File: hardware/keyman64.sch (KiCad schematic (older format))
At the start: 28 parts, among them IC1 ATMEGA1284P-P, P1 SERIAL, P2 CIA1, P3 KEYBOARD, P4 USER, P6 USB, SW1 RESET, SW2 BOOTLOADER, SW3 POWER, U1 7400, U2 ICL7660, U3 4520, U4 4051, U5 4051, U6 CD74HC22106, X1 16Mhz

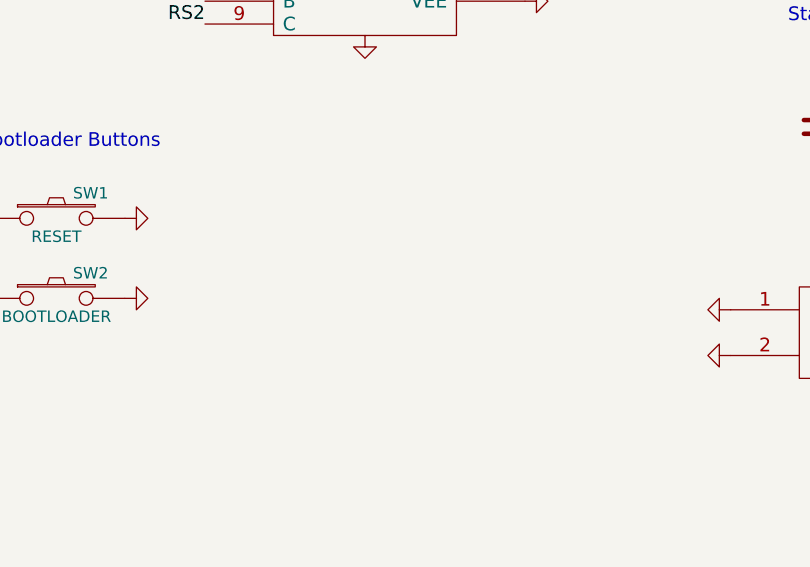
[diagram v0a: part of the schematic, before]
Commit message: Hardware: Increased board height to 6,4cm to make room for mounting holes
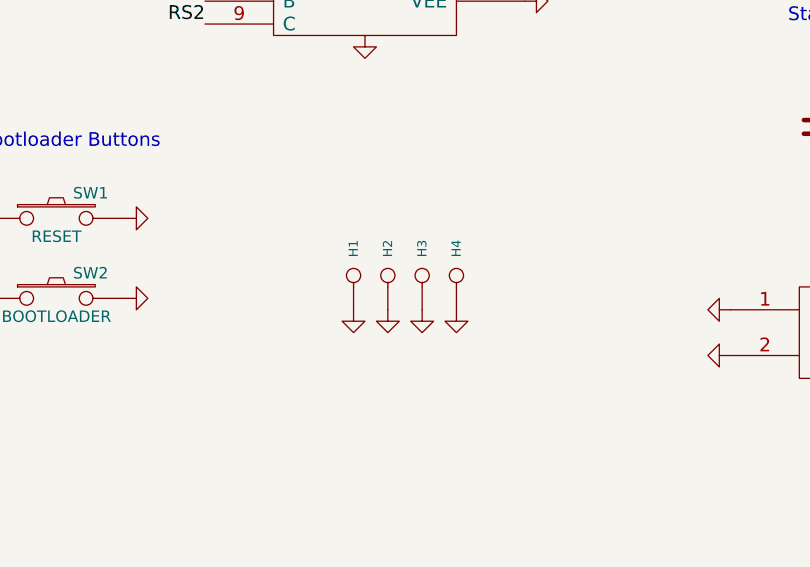
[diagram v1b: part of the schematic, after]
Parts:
- added H1, H2, H3, H4: CONN_1, symbol CONN_1
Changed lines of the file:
@@
 Sheet 1 1
 Title "Programmable C64 Keyboard Interceptor and Hardware Controller"
-Date "23 oct 2015"
+Date "24 oct 2015"
 Rev "2"
 Comp "Henning Bekel"
@@
 Text Label 900  2950 2    60   ~ 0
 KVCC
+$Comp
+L CONN_1 H1
+U 1 1 562B9608
+P 8150 6500
+F 0 "H1" H 8230 6500 40  0000 L CNN
+F 1 "CONN_1" H 8150 6555 30  0001 C CNN
+F 2 "" H 8150 6500 60  0000 C CNN
+F 3 "" H 8150 6500 60  0000 C CNN
+	1    8150 6500
+	0    -1   -1   0
+$EndComp
+$Comp
+L GND #PWR046
+U 1 1 562B9617
+P 8150 6650
+F 0 "#PWR046" H 8150 6650 30  0001 C CNN
+F 1 "GND" H 8150 6580 30  0001 C CNN
+F 2 "" H 8150 6650 60  0000 C CNN
+F 3 "" H 8150 6650 60  0000 C CNN
+	1    8150 6650
+	1    0    0    -1
+$EndComp
+$Comp
+L CONN_1 H2
+U 1 1 562B962E
+P 8300 6500
+F 0 "H2" H 8380 6500 40  0000 L CNN
+F 1 "CONN_1" H 8300 6555 30  0001 C CNN
+F 2 "" H 8300 6500 60  0000 C CNN
+F 3 "" H 8300 6500 60  0000 C CNN
+	1    8300 6500
+	0    -1   -1   0
+$EndComp
+$Comp
+L GND #PWR047
+U 1 1 562B9634
+P 8300 6650
+F 0 "#PWR047" H 8300 6650 30  0001 C CNN
+F 1 "GND" H 8300 6580 30  0001 C CNN
+F 2 "" H 8300 6650 60  0000 C CNN
+F 3 "" H 8300 6650 60  0000 C CNN
+	1    8300 6650
+	1    0    0    -1
+$EndComp
+$Comp
+L CONN_1 H3
+U 1 1 562B963A
+P 8450 6500
+F 0 "H3" H 8530 6500 40  0000 L CNN
+F 1 "CONN_1" H 8450 6555 30  0001 C CNN
+F 2 "" H 8450 6500 60  0000 C CNN
+F 3 "" H 8450 6500 60  0000 C CNN
+	1    8450 6500
+	0    -1   -1   0
+$EndComp
+$Comp
+L GND #PWR048
+U 1 1 562B9640
+P 8450 6650
+F 0 "#PWR048" H 8450 6650 30  0001 C CNN
+F 1 "GND" H 8450 6580 30  0001 C CNN
+F 2 "" H 8450 6650 60  0000 C CNN
+F 3 "" H 8450 6650 60  0000 C CNN
+	1    8450 6650
+	1    0    0    -1
+$EndComp
+$Comp
+L CONN_1 H4
+U 1 1 562B9646
+P 8600 6500
+F 0 "H4" H 8680 6500 40  0000 L CNN
+F 1 "CONN_1" H 8600 6555 30  0001 C CNN
+F 2 "" H 8600 6500 60  0000 C CNN
+F 3 "" H 8600 6500 60  0000 C CNN
+	1    8600 6500
+	0    -1   -1   0
+$EndComp
+$Comp
+L GND #PWR049
+U 1 1 562B964C
+P 8600 6650
+F 0 "#PWR049" H 8600 6650 30  0001 C CNN
+F 1 "GND" H 8600 6580 30  0001 C CNN
+F 2 "" H 8600 6650 60  0000 C CNN
+F 3 "" H 8600 6650 60  0000 C CNN
+	1    8600 6650
+	1    0    0    -1
+$EndComp
 $EndSCHEMATC

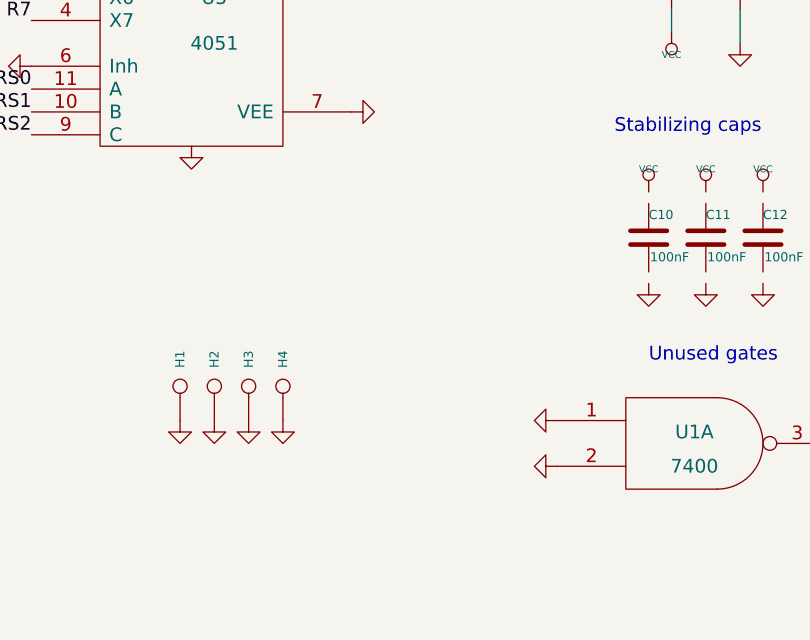
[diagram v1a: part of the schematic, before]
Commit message: Hardware: Rearranged parts, more caps, rerouted (first rough draft)
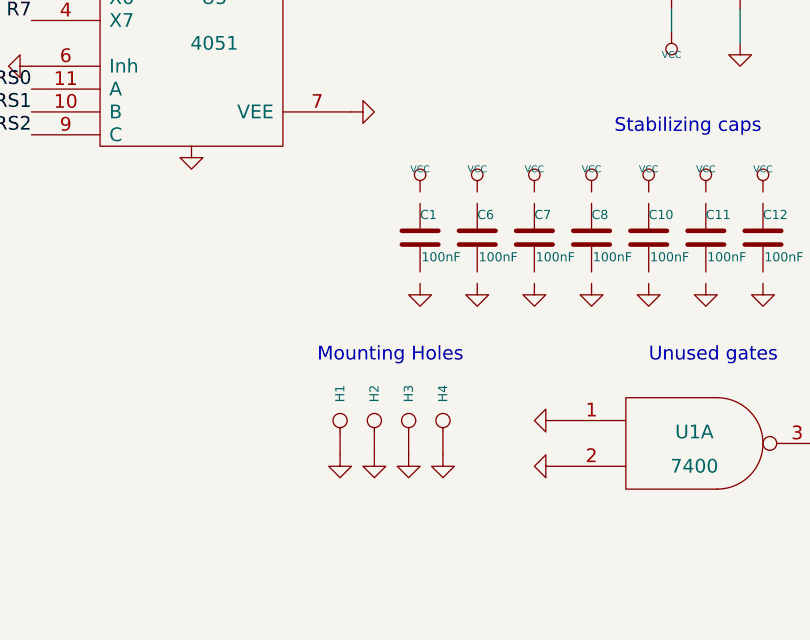
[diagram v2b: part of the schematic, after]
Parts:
- added C1, C6, C7, C8: 100nF, ~, symbol C
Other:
- note added: "Mounting Holes"
- moved on the sheet: H1, H2, H3, H4
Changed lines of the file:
@@
 Sheet 1 1
 Title "Programmable C64 Keyboard Interceptor and Hardware Controller"
-Date "24 oct 2015"
+Date "27 oct 2015"
 Rev "2"
 Comp "Henning Bekel"
@@
 	1    0    0    -1
 $EndComp
-NoConn ~ 900  2200
 Text Label 900  2000 2    60   ~ 0
 D-
@@
 L CONN_1 H1
 U 1 1 562B9608
-P 8150 6500
-F 0 "H1" H 8230 6500 40  0000 L CNN
-F 1 "CONN_1" H 8150 6555 30  0001 C CNN
-F 2 "" H 8150 6500 60  0000 C CNN
-F 3 "" H 8150 6500 60  0000 C CNN
-	1    8150 6500
+P 8850 6650
+F 0 "H1" H 8930 6650 40  0000 L CNN
+F 1 "CONN_1" H 8850 6705 30  0001 C CNN
+F 2 "" H 8850 6650 60  0000 C CNN
+F 3 "" H 8850 6650 60  0000 C CNN
+	1    8850 6650
 	0    -1   -1   0
 $EndComp
@@
 L GND #PWR046
 U 1 1 562B9617
-P 8150 6650
-F 0 "#PWR046" H 8150 6650 30  0001 C CNN
-F 1 "GND" H 8150 6580 30  0001 C CNN
-F 2 "" H 8150 6650 60  0000 C CNN
-F 3 "" H 8150 6650 60  0000 C CNN
-	1    8150 6650
+P 8850 6800
+F 0 "#PWR046" H 8850 6800 30  0001 C CNN
+F 1 "GND" H 8850 6730 30  0001 C CNN
+F 2 "" H 8850 6800 60  0000 C CNN
+F 3 "" H 8850 6800 60  0000 C CNN
+	1    8850 6800
 	1    0    0    -1
 $EndComp
@@
 L CONN_1 H2
 U 1 1 562B962E
-P 8300 6500
-F 0 "H2" H 8380 6500 40  0000 L CNN
-F 1 "CONN_1" H 8300 6555 30  0001 C CNN
-F 2 "" H 8300 6500 60  0000 C CNN
-F 3 "" H 8300 6500 60  0000 C CNN
-	1    8300 6500
+P 9000 6650
+F 0 "H2" H 9080 6650 40  0000 L CNN
+F 1 "CONN_1" H 9000 6705 30  0001 C CNN
+F 2 "" H 9000 6650 60  0000 C CNN
+F 3 "" H 9000 6650 60  0000 C CNN
+	1    9000 6650
 	0    -1   -1   0
 $EndComp
@@
 L GND #PWR047
 U 1 1 562B9634
-P 8300 6650
-F 0 "#PWR047" H 8300 6650 30  0001 C CNN
-F 1 "GND" H 8300 6580 30  0001 C CNN
-F 2 "" H 8300 6650 60  0000 C CNN
-F 3 "" H 8300 6650 60  0000 C CNN
-	1    8300 6650
+P 9000 6800
+F 0 "#PWR047" H 9000 6800 30  0001 C CNN
+F 1 "GND" H 9000 6730 30  0001 C CNN
+F 2 "" H 9000 6800 60  0000 C CNN
+F 3 "" H 9000 6800 60  0000 C CNN
+	1    9000 6800
 	1    0    0    -1
 $EndComp
@@
 L CONN_1 H3
 U 1 1 562B963A
-P 8450 6500
-F 0 "H3" H 8530 6500 40  0000 L CNN
-F 1 "CONN_1" H 8450 6555 30  0001 C CNN
-F 2 "" H 8450 6500 60  0000 C CNN
-F 3 "" H 8450 6500 60  0000 C CNN
-	1    8450 6500
+P 9150 6650
+F 0 "H3" H 9230 6650 40  0000 L CNN
+F 1 "CONN_1" H 9150 6705 30  0001 C CNN
+F 2 "" H 9150 6650 60  0000 C CNN
+F 3 "" H 9150 6650 60  0000 C CNN
+	1    9150 6650
 	0    -1   -1   0
 $EndComp
@@
 L GND #PWR048
 U 1 1 562B9640
-P 8450 6650
-F 0 "#PWR048" H 8450 6650 30  0001 C CNN
-F 1 "GND" H 8450 6580 30  0001 C CNN
-F 2 "" H 8450 6650 60  0000 C CNN
-F 3 "" H 8450 6650 60  0000 C CNN
-	1    8450 6650
+P 9150 6800
+F 0 "#PWR048" H 9150 6800 30  0001 C CNN
+F 1 "GND" H 9150 6730 30  0001 C CNN
+F 2 "" H 9150 6800 60  0000 C CNN
+F 3 "" H 9150 6800 60  0000 C CNN
+	1    9150 6800
 	1    0    0    -1
 $EndComp
@@
 L CONN_1 H4
 U 1 1 562B9646
-P 8600 6500
-F 0 "H4" H 8680 6500 40  0000 L CNN
-F 1 "CONN_1" H 8600 6555 30  0001 C CNN
-F 2 "" H 8600 6500 60  0000 C CNN
-F 3 "" H 8600 6500 60  0000 C CNN
-	1    8600 6500
+P 9300 6650
+F 0 "H4" H 9380 6650 40  0000 L CNN
+F 1 "CONN_1" H 9300 6705 30  0001 C CNN
+F 2 "" H 9300 6650 60  0000 C CNN
+F 3 "" H 9300 6650 60  0000 C CNN
+	1    9300 6650
 	0    -1   -1   0
 $EndComp
@@
 L GND #PWR049
 U 1 1 562B964C
-P 8600 6650
-F 0 "#PWR049" H 8600 6650 30  0001 C CNN
-F 1 "GND" H 8600 6580 30  0001 C CNN
-F 2 "" H 8600 6650 60  0000 C CNN
-F 3 "" H 8600 6650 60  0000 C CNN
-	1    8600 6650
-	1    0    0    -1
-$EndComp
+P 9300 6800
+F 0 "#PWR049" H 9300 6800 30  0001 C CNN
+F 1 "GND" H 9300 6730 30  0001 C CNN
+F 2 "" H 9300 6800 60  0000 C CNN
+F 3 "" H 9300 6800 60  0000 C CNN
+	1    9300 6800
+	1    0    0    -1
+$EndComp
+$Comp
+L C C7
+U 1 1 562F7DD8
+P 9700 5850
+F 0 "C7" H 9700 5950 40  0000 L CNN
+F 1 "100nF" H 9706 5765 40  0000 L CNN
+F 2 "~" H 9738 5700 30  0000 C CNN
+F 3 "~" H 9700 5850 60  0000 C CNN
+	1    9700 5850
+	1    0    0    -1
+$EndComp
+$Comp
+L VCC #PWR050
+U 1 1 562F7DDE
+P 9700 5650
+F 0 "#PWR050" H 9700 5750 30  0001 C CNN
+F 1 "VCC" H 9700 5750 30  0000 C CNN
+F 2 "" H 9700 5650 60  0000 C CNN
+F 3 "" H 9700 5650 60  0000 C CNN
+	1    9700 5650
+	1    0    0    -1
+$EndComp
+$Comp
+L GND #PWR051
+U 1 1 562F7DE4
+P 9700 6050
+F 0 "#PWR051" H 9700 6050 30  0001 C CNN
+F 1 "GND" H 9700 5980 30  0001 C CNN
+F 2 "" H 9700 6050 60  0000 C CNN
+F 3 "" H 9700 6050 60  0000 C CNN
+	1    9700 6050
+	1    0    0    -1
+$EndComp
+$Comp
+L C C8
+U 1 1 562F7DEA
+P 9950 5850
+F 0 "C8" H 9950 5950 40  0000 L CNN
+F 1 "100nF" H 9956 5765 40  0000 L CNN
+F 2 "~" H 9988 5700 30  0000 C CNN
+F 3 "~" H 9950 5850 60  0000 C CNN
+	1    9950 5850
+	1    0    0    -1
+$EndComp
+$Comp
+L VCC #PWR052
+U 1 1 562F7DF0
+P 9950 5650
+F 0 "#PWR052" H 9950 5750 30  0001 C CNN
+F 1 "VCC" H 9950 5750 30  0000 C CNN
+F 2 "" H 9950 5650 60  0000 C CNN
+F 3 "" H 9950 5650 60  0000 C CNN
+	1    9950 5650
+	1    0    0    -1
+$EndComp
+$Comp
+L GND #PWR053
+U 1 1 562F7DF6
+P 9950 6050
+F 0 "#PWR053" H 9950 6050 30  0001 C CNN
+F 1 "GND" H 9950 5980 30  0001 C CNN
+F 2 "" H 9950 6050 60  0000 C CNN
+F 3 "" H 9950 6050 60  0000 C CNN
+	1    9950 6050
+	1    0    0    -1
+$EndComp
+$Comp
+L C C1
+U 1 1 562F7DFC
+P 9200 5850
+F 0 "C1" H 9200 5950 40  0000 L CNN
+F 1 "100nF" H 9206 5765 40  0000 L CNN
+F 2 "~" H 9238 5700 30  0000 C CNN
+F 3 "~" H 9200 5850 60  0000 C CNN
+	1    9200 5850
+	1    0    0    -1
+$EndComp
+$Comp
+L VCC #PWR054
+U 1 1 562F7E02
+P 9200 5650
+F 0 "#PWR054" H 9200 5750 30  0001 C CNN
+F 1 "VCC" H 9200 5750 30  0000 C CNN
+F 2 "" H 9200 5650 60  0000 C CNN
+F 3 "" H 9200 5650 60  0000 C CNN
+	1    9200 5650
+	1    0    0    -1
+$EndComp
+$Comp
+L GND #PWR055
+U 1 1 562F7E08
+P 9200 6050
+F 0 "#PWR055" H 9200 6050 30  0001 C CNN
+F 1 "GND" H 9200 5980 30  0001 C CNN
+F 2 "" H 9200 6050 60  0000 C CNN
+F 3 "" H 9200 6050 60  0000 C CNN
+	1    9200 6050
+	1    0    0    -1
+$EndComp
+$Comp
+L C C6
+U 1 1 562F7E0E
+P 9450 5850
+F 0 "C6" H 9450 5950 40  0000 L CNN
+F 1 "100nF" H 9456 5765 40  0000 L CNN
+F 2 "~" H 9488 5700 30  0000 C CNN
+F 3 "~" H 9450 5850 60  0000 C CNN
+	1    9450 5850
+	1    0    0    -1
+$EndComp
+$Comp
+L VCC #PWR056
+U 1 1 562F7E14
+P 9450 5650
+F 0 "#PWR056" H 9450 5750 30  0001 C CNN
+F 1 "VCC" H 9450 5750 30  0000 C CNN
+F 2 "" H 9450 5650 60  0000 C CNN
+F 3 "" H 9450 5650 60  0000 C CNN
+	1    9450 5650
+	1    0    0    -1
+$EndComp
+$Comp
+L GND #PWR057
+U 1 1 562F7E1A
+P 9450 6050
+F 0 "#PWR057" H 9450 6050 30  0001 C CNN
+F 1 "GND" H 9450 5980 30  0001 C CNN
+F 2 "" H 9450 6050 60  0000 C CNN
+F 3 "" H 9450 6050 60  0000 C CNN
+	1    9450 6050
+	1    0    0    -1
+$EndComp
+NoConn ~ 900  2200
+Text Notes 8750 6400 0    60   ~ 0
+Mounting Holes
 $EndSCHEMATC

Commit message: Hardware: Ported to KiCAD 4.0.0-rc2 format, improved routing and screen
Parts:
- C1, C10, C11, C12, C6, C7, C8: footprint ~ -> Capacitors_ThroughHole:C_Disc_D3_P2.5; symbol C -> C-RESCUE-keyman64
- C2, C3: value 18nF -> 18pF; footprint ~ -> Capacitors_ThroughHole:C_Disc_D3_P2.5; symbol C -> C-RESCUE-keyman64
- C4, C5: footprint ~ -> Capacitors_ThroughHole:C_Disc_D3_P2.5; symbol CP1 -> CP1-RESCUE-keyman64
- D1, D2: footprint (none) -> Diode:Diode-2.5mm-Vertical; symbol ZENER -> ZENER-RESCUE-keyman64
- H1, H2, H3, H4: footprint (none) -> Mounting_Holes:MountingHole_3mm
- IC1: value ATMEGA1284P-P -> ATMEGA1284P-PU; footprint DIL40 -> Sockets_DIP:DIP-40__600
- P1: footprint (none) -> pinHeaders:pinHeader-2x1
- P2: value CIA1 -> COMPUTER; footprint (none) -> pinHeaders:pinHeader-20x1
- P3: footprint (none) -> pinHeaders:pinHeader-20x1
- P4: value USER -> CONTROL; footprint (none) -> pinHeaders:pin_array_8x2
- P6: footprint (none) -> usb-mini-b-through-hole:USB-MINI-B-H
- R2, R3, R4: footprint (none) -> Discret:R1; symbol R -> R-RESCUE-keyman64
- SW1: footprint (none) -> Buttons_Switches_ThroughHole:SW_PUSH_SMALL
- SW2: value BOOTLOADER -> BOOT; footprint (none) -> Buttons_Switches_ThroughHole:SW_PUSH_SMALL
- SW3: footprint ~ -> pinHeaders:pinHeader-3x1
- U1: footprint ~ -> Sockets_DIP:DIP-14__300
- U2: value ICL7660 -> 7660; footprint (none) -> Sockets_DIP:DIP-8__300
- U3, U4, U5: footprint (none) -> Sockets_DIP:DIP-16__300
- U6: value CD74HC22106 -> CD74HC22106/MT8808; footprint (none) -> Sockets_DIP:DIP-28__600
- X1: value 16Mhz -> 16MHz; footprint ~ -> Crystals:HC-49V
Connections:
- no-connect marks 8 -> 12
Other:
- moved on the sheet: C1, C10, C11, C12, C6, C7, C8, H1, H2, H3, H4, SW1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

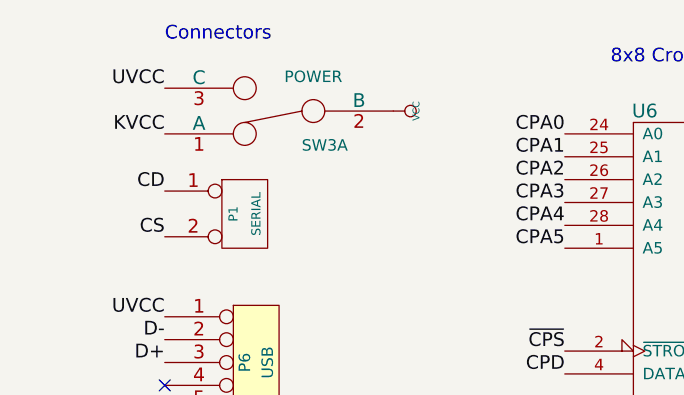
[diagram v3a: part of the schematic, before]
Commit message: Hardware: Use single switch component for power jumper instead of double
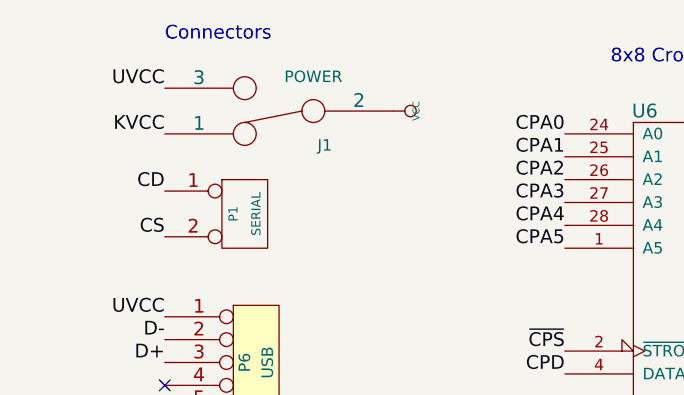
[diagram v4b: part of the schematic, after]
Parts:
- removed SW3: POWER, pinHeaders:pinHeader-3x1, symbol DUAL_SWITCH_INV
- added J1: POWER, pinHeaders:pinHeader-3x1, symbol SWITCH_INV
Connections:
- net KVCC: now also J1.1
- net UVCC: now also J1.3
- net VCC: now also J1.2
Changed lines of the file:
@@
 EESchema Schematic File Version 2
-LIBS:keyman64-rescue
 LIBS:power
 LIBS:device
@@
 LIBS:valves
 LIBS:cd74hc22106
+LIBS:legacy
 LIBS:keyman64-cache
 EELAYER 25 0
@@
 	0    1    1    0
 $EndComp
-$Comp
-L DUAL_SWITCH_INV SW3
-U 1 1 562A2E46
-P 1400 1000
-F 0 "SW3" H 1200 1150 50  0000 C CNN
-F 1 "POWER" H 1250 850 50  0000 C CNN
-F 2 "pinHeaders:pinHeader-3x1" H 1400 1000 60  0001 C CNN
-F 3 "~" H 1400 1000 60  0000 C CNN
-	1    1400 1000
-	-1   0    0    1
-$EndComp
 Text Label 900  1100 2    60   ~ 0
 KVCC
@@
 NoConn ~ 10600 5000
 NoConn ~ 10450 5000
+$Comp
+L SWITCH_INV J1
+U 1 1 564C829F
+P 1400 1000
+F 0 "J1" H 1200 1150 50  0000 C CNN
+F 1 "POWER" H 1250 850 50  0000 C CNN
+F 2 "pinHeaders:pinHeader-3x1" H 1400 1000 60  0001 C CNN
+F 3 "" H 1400 1000 60  0000 C CNN
+	1    1400 1000
+	-1   0    0    1
+$EndComp
 $EndSCHEMATC
